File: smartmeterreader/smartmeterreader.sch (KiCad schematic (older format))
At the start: 5 parts

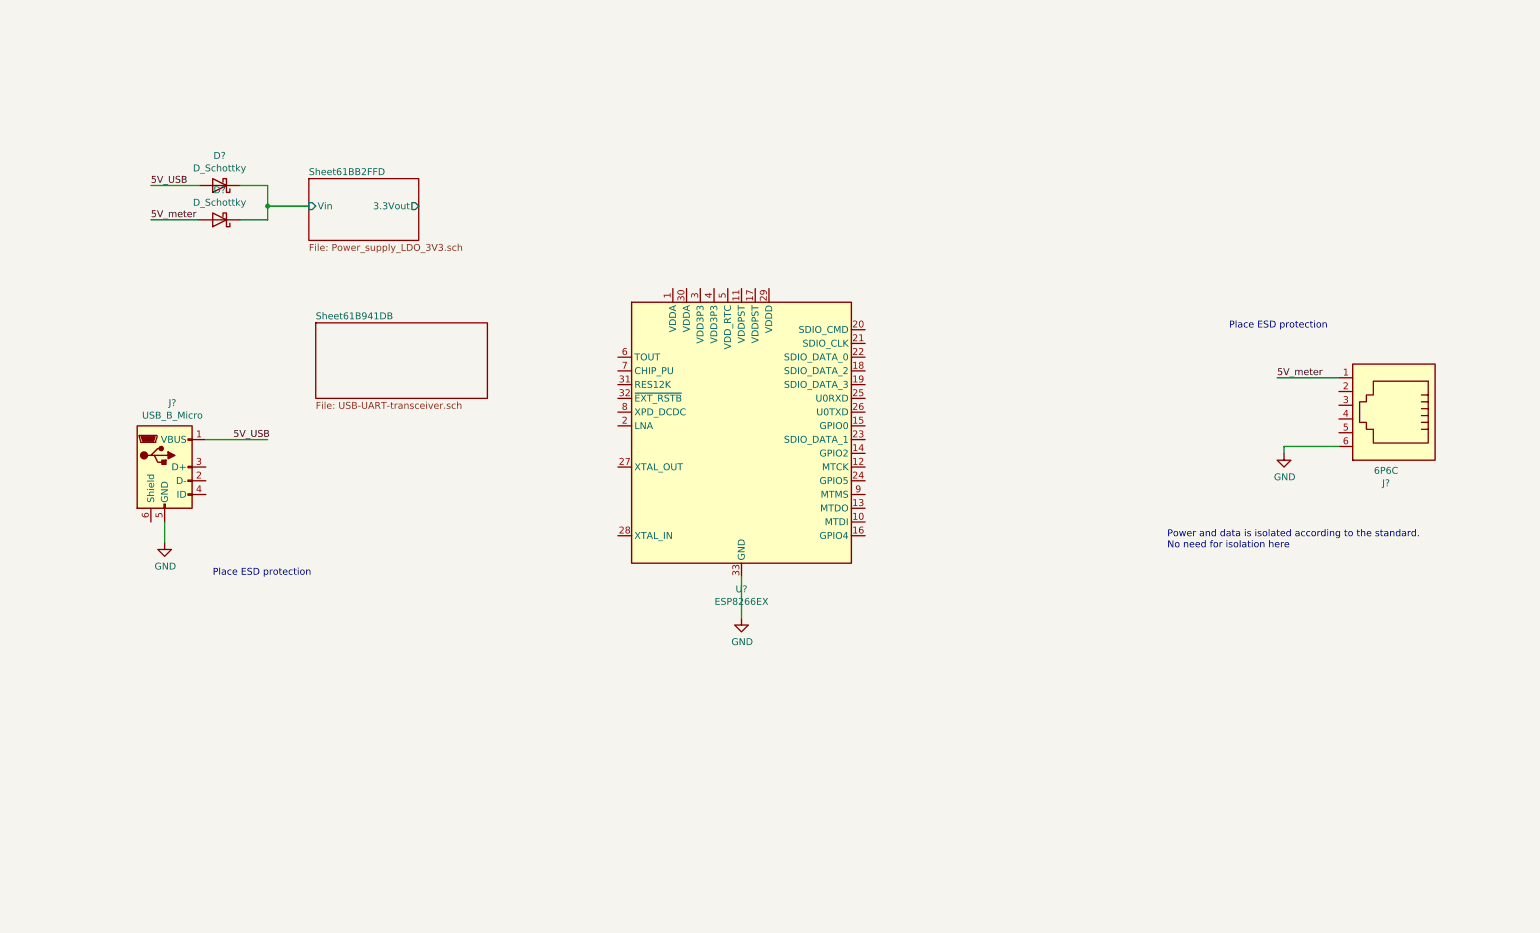
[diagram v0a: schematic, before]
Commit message: Initial version of the smart meter. -Needs compoonent review, - Needs schematics review - No layout
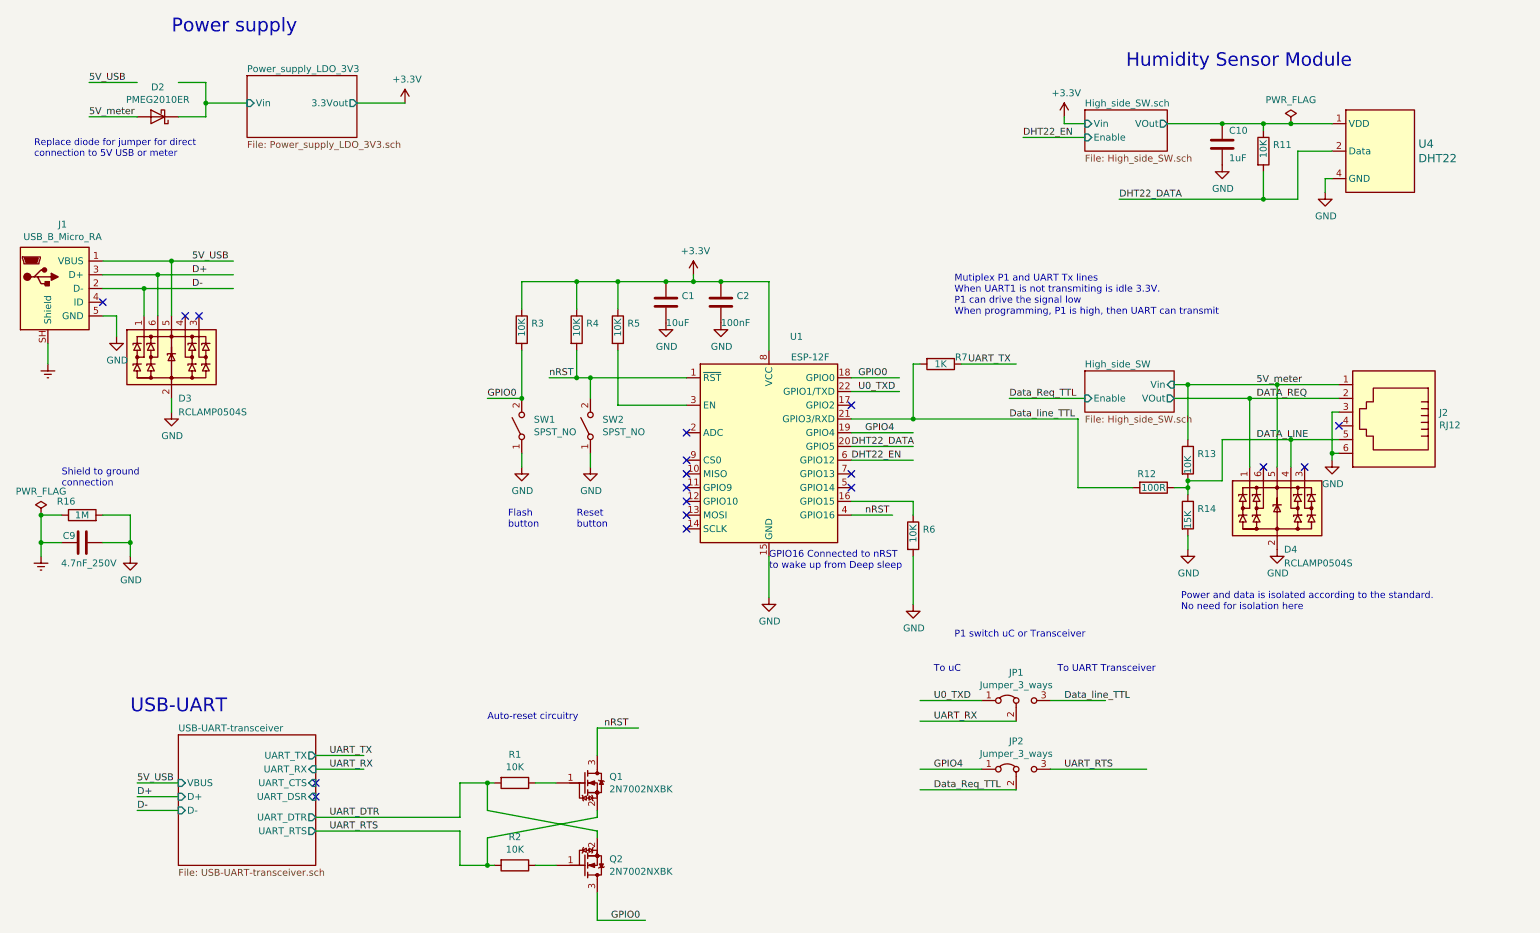
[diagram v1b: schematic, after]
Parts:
- removed D? (x2): D_Schottky, symbol Device:D_Schottky
- removed J?: 6P6C, symbol Connector:6P6C
- removed J?: USB_B_Micro, symbol Connector:USB_B_Micro
- removed U?: ESP8266EX, Package_DFN_QFN:QFN-32-1EP_5x5mm_P0.5mm_EP3.45x3.45mm, symbol MCU_Espressif:ESP8266EX
- added C1: 10uF, Capacitor_SMD:C_0805_2012Metric, symbol Capacitor_Ceramic_SMD_0603:10uF
- added C10: 1uF, Capacitor_SMD:C_0603_1608Metric_Pad1.08x0.95mm_HandSolder, symbol Capacitor_Ceramic_SMD_0603:1uF
- added C2: 100nF, Capacitor_SMD:C_0603_1608Metric_Pad1.08x0.95mm_HandSolder, symbol Capacitor_Ceramic_SMD_0603:100nF
- added C9: 4.7nF_250V, Capacitor_SMD:C_0805_2012Metric, symbol Capacitor_Ceramic_SMD_0603:4.7nF_250V
- added D2: PMEG2010ER, Diode_SMD:D_SOD-123, symbol Diode_SMD:PMEG2010ER
- added D3, D4: RCLAMP0504S, Package_TO_SOT_SMD:SOT-23-6, symbol Diode_SMD:RCLAMP0504S
- added J1: USB_B_Micro_RA, Connector_digital:USB_Micro_B_Female_10118193-0001LF, symbol CON:USB_B_Micro_RA
- added J2: RJ12, Connector_digital:RJ12_Amphenol_54601, symbol Connector_THT:RJ12
- added JP1, JP2: Jumper_3_ways, Connector_PinHeader_2.54mm:PinHeader_1x03_P2.54mm_Vertical, symbol Connector_THT:Jumper_3_ways
- added Q1, Q2: 2N7002NXBK, Package_TO_SOT_SMD:SOT-23, symbol Transistor:2N7002NXBK
- added R1, R11, R13, R2, R3, R4, R5, R6: 10K, Resistor_SMD:R_0603_1608Metric, symbol Resistor_SMD_0603:10K
- added R12: 100R, Resistor_SMD:R_0603_1608Metric, symbol Resistor_SMD_0603:100R
- added R14: 15K, Resistor_SMD:R_0603_1608Metric, symbol Resistor_SMD_0603:15K
- added R16: 1M, Resistor_SMD:R_0603_1608Metric, symbol Resistor_SMD_0603:1M
- added R7: 1K, Resistor_SMD:R_0603_1608Metric, symbol Resistor_SMD_0603:1K
- added SW1, SW2: SPST_NO, MECH_Switch_SMD:SW_Push_1P1T_NO_CK_KMR2, symbol MECH_Switch_SMD:SPST_NO
- added U1: ESP-12F, RF_Module:ESP-12E, symbol IC_Digital:ESP-12F
- added U4: DHT22, Modules:DHT22_7.7x15.1_P2mm, symbol IC_Analog:DHT22
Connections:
- net labels added: +3.3V, D+, D-, DATA_LINE, DATA_REQ, DHT22_DATA, DHT22_EN, Data_Req_TTL, Data_line_TTL, Earth, GPIO0, GPIO4, U0_TXD, UART_DTR, UART_RTS, UART_RX, UART_TX, nRST
- wire segments 13 -> 136
- no-connect marks 0 -> 18
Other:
- note added: "Auto-reset circuitry"
- note added: "Flash\nbutton"
- note added: "GPIO16 Connected to nRST \nto wake up from Deep sleep"
- note added: "Humidity Sensor Module"
- note added: "Mutiplex P1 and UART Tx lines\nWhen UART1 is not transmiting is idle 3.3V. \nP1 can drive the signal low \nWhen programming, P1 is high, then UART can transmit"
- note added: "P1 switch uC or Transceiver\n"
- note added: "Power supply"
- note added: "Replace diode for jumper for direct \nconnection to 5V USB or meter"
- note added: "Reset\nbutton"
- note added: "Shield to ground \nconnection"
- note added: "To UART Transceiver"
- note added: "To uC"
- note added: "USB-UART"
- note removed: "Place ESD protection"
